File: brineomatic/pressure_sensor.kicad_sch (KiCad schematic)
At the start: 5 parts

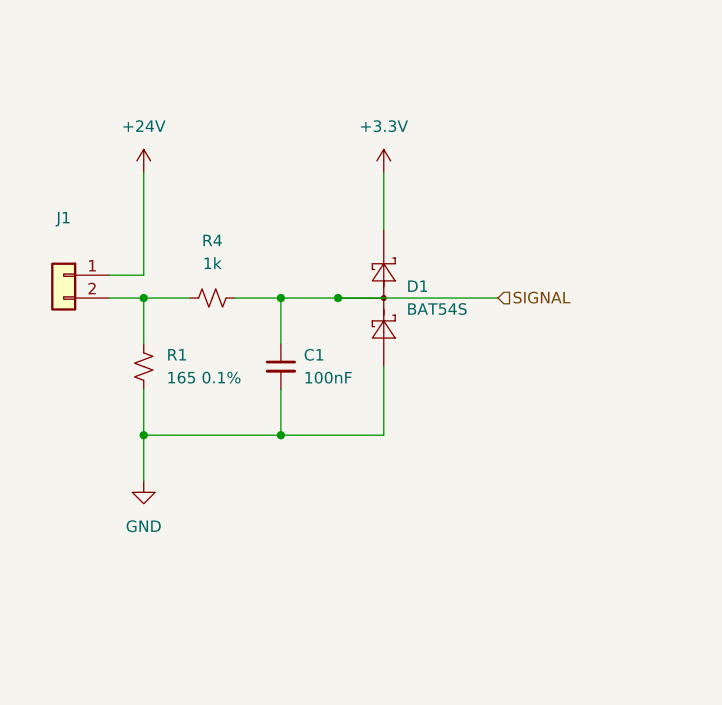
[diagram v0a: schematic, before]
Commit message: switched to onboard esp32-s3 and re-drew tmc2209 driver
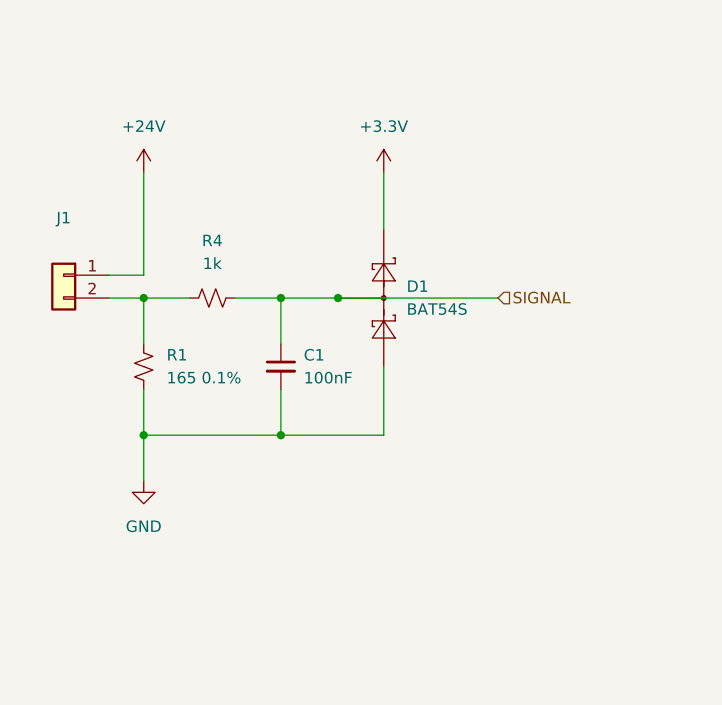
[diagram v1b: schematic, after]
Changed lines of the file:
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@@
 			)
 		)
-		(property "Description" ""
+		(property "Description" "Resistor, small US symbol"
 			(at 104.14 87.63 0)
 			(effects
@@
 		(fields_autoplaced yes)
 		(property "Reference" "R1"
-			(at 99.06 93.98 0)
+			(at 99.06 93.9799 0)
 			(effects
 				(font
@@
 		)
 		(property "Value" "165 0.1%"
-			(at 99.06 96.52 0)
+			(at 99.06 96.5199 0)
 			(effects
 				(font
@@
 			)
 		)
-		(property "Description" ""
+		(property "Description" "Resistor, small US symbol"
 			(at 96.52 95.25 0)
 			(effects

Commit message: tmc2209 driver schematic checked and laid out nicely.
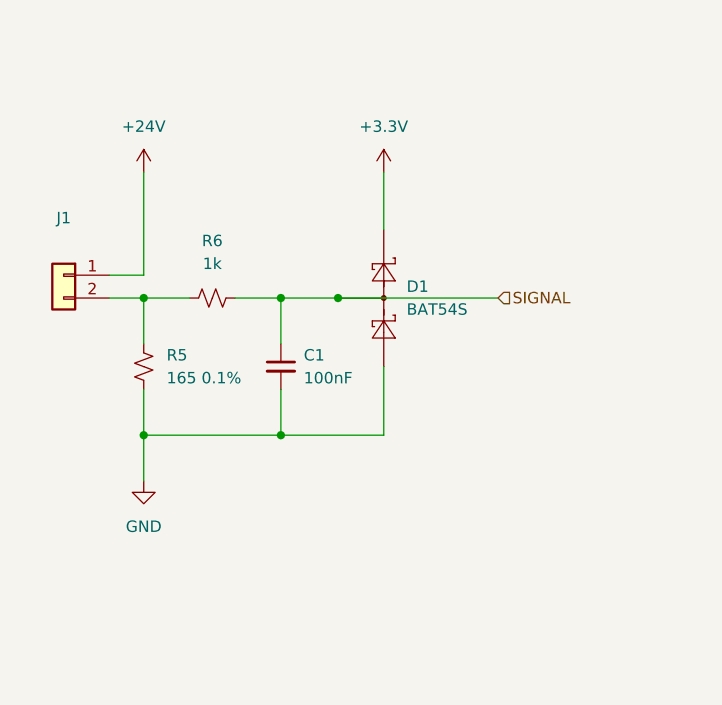
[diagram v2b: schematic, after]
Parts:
- renumbered R1 to R5, R4 to R6
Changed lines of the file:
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@@
 		(dnp no)
 		(fields_autoplaced yes)
-		(property "Reference" "#PWR06"
+		(property "Reference" "#PWR07"
 			(at 96.52 77.47 0)
 			(effects
@@
 			(project "brineomatic"
 				(path "/96477ae2-ef08-48f3-8dd4-fe4478541f68/c8ab4709-9ad5-4833-bb93-07e00d6a0170"
-					(reference "#PWR035")
-					(unit 1)
-				)
-				(path "/96477ae2-ef08-48f3-8dd4-fe4478541f68/e7fd98b0-0753-4e9e-b57d-135c0c1a0b39"
-					(reference "#PWR06")
+					(reference "#PWR039")
+					(unit 1)
+				)
+				(path "/96477ae2-ef08-48f3-8dd4-fe4478541f68/e7fd98b0-0753-4e9e-b57d-135c0c1a0b39"
+					(reference "#PWR07")
 					(unit 1)
 				)
@@
 		(dnp no)
 		(fields_autoplaced yes)
-		(property "Reference" "#PWR08"
+		(property "Reference" "#PWR09"
 			(at 123.19 77.47 0)
 			(effects
@@
 			(project "brineomatic"
 				(path "/96477ae2-ef08-48f3-8dd4-fe4478541f68/c8ab4709-9ad5-4833-bb93-07e00d6a0170"
-					(reference "#PWR037")
-					(unit 1)
-				)
-				(path "/96477ae2-ef08-48f3-8dd4-fe4478541f68/e7fd98b0-0753-4e9e-b57d-135c0c1a0b39"
-					(reference "#PWR08")
+					(reference "#PWR041")
+					(unit 1)
+				)
+				(path "/96477ae2-ef08-48f3-8dd4-fe4478541f68/e7fd98b0-0753-4e9e-b57d-135c0c1a0b39"
+					(reference "#PWR09")
 					(unit 1)
 				)
@@
 		(dnp no)
 		(fields_autoplaced yes)
-		(property "Reference" "#PWR07"
+		(property "Reference" "#PWR08"
 			(at 96.52 114.3 0)
 			(effects
@@
 			(project "brineomatic"
 				(path "/96477ae2-ef08-48f3-8dd4-fe4478541f68/c8ab4709-9ad5-4833-bb93-07e00d6a0170"
-					(reference "#PWR036")
-					(unit 1)
-				)
-				(path "/96477ae2-ef08-48f3-8dd4-fe4478541f68/e7fd98b0-0753-4e9e-b57d-135c0c1a0b39"
-					(reference "#PWR07")
+					(reference "#PWR040")
+					(unit 1)
+				)
+				(path "/96477ae2-ef08-48f3-8dd4-fe4478541f68/e7fd98b0-0753-4e9e-b57d-135c0c1a0b39"
+					(reference "#PWR08")
 					(unit 1)
 				)
@@
 			(project "brineomatic"
 				(path "/96477ae2-ef08-48f3-8dd4-fe4478541f68/c8ab4709-9ad5-4833-bb93-07e00d6a0170"
-					(reference "D18")
+					(reference "D19")
 					(unit 1)
 				)
@@
 			(project "brineomatic"
 				(path "/96477ae2-ef08-48f3-8dd4-fe4478541f68/c8ab4709-9ad5-4833-bb93-07e00d6a0170"
-					(reference "J12")
+					(reference "J17")
 					(unit 1)
 				)
@@
 		(dnp no)
 		(fields_autoplaced yes)
-		(property "Reference" "R4"
+		(property "Reference" "R6"
 			(at 104.14 81.28 90)
 			(effects
@@
 				)
 				(path "/96477ae2-ef08-48f3-8dd4-fe4478541f68/e7fd98b0-0753-4e9e-b57d-135c0c1a0b39"
-					(reference "R4")
+					(reference "R6")
 					(unit 1)
 				)
@@
 		(dnp no)
 		(fields_autoplaced yes)
-		(property "Reference" "R1"
+		(property "Reference" "R5"
 			(at 99.06 93.9799 0)
 			(effects
@@
 			(project "brineomatic"
 				(path "/96477ae2-ef08-48f3-8dd4-fe4478541f68/c8ab4709-9ad5-4833-bb93-07e00d6a0170"
-					(reference "R31")
-					(unit 1)
-				)
-				(path "/96477ae2-ef08-48f3-8dd4-fe4478541f68/e7fd98b0-0753-4e9e-b57d-135c0c1a0b39"
-					(reference "R1")
+					(reference "R33")
+					(unit 1)
+				)
+				(path "/96477ae2-ef08-48f3-8dd4-fe4478541f68/e7fd98b0-0753-4e9e-b57d-135c0c1a0b39"
+					(reference "R5")
 					(unit 1)
 				)
@@
 			(project "brineomatic"
 				(path "/96477ae2-ef08-48f3-8dd4-fe4478541f68/c8ab4709-9ad5-4833-bb93-07e00d6a0170"
-					(reference "C17")
-					(unit 1)
-				)
+					(reference "C14")
+					(unit 1)
+				)

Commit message: worked on bom for rev b prototype run
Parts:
- C1: LCSC C49678 -> (none)
- R6: LCSC C95781 -> (none)
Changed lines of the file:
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@@
 			)
 		)
-		(property "LCSC" "C95781"
+		(property "LCSC" ""
 			(at 104.14 87.63 0)
 			(effects
@@
 			)
 		)
-		(property "LCSC" "C49678"
+		(property "LCSC" ""
 			(at 111.76 95.25 0)
 			(effects

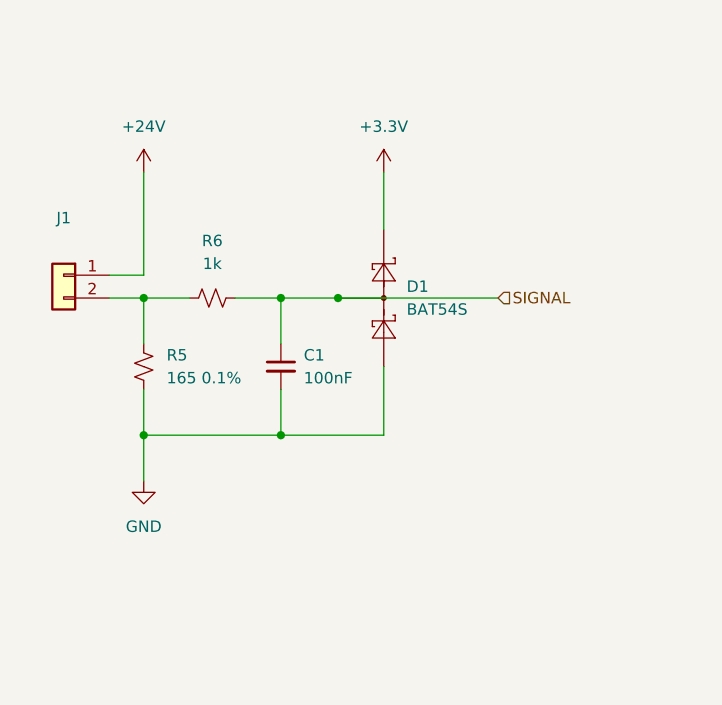
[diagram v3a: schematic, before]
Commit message: added qwiic i2c connector
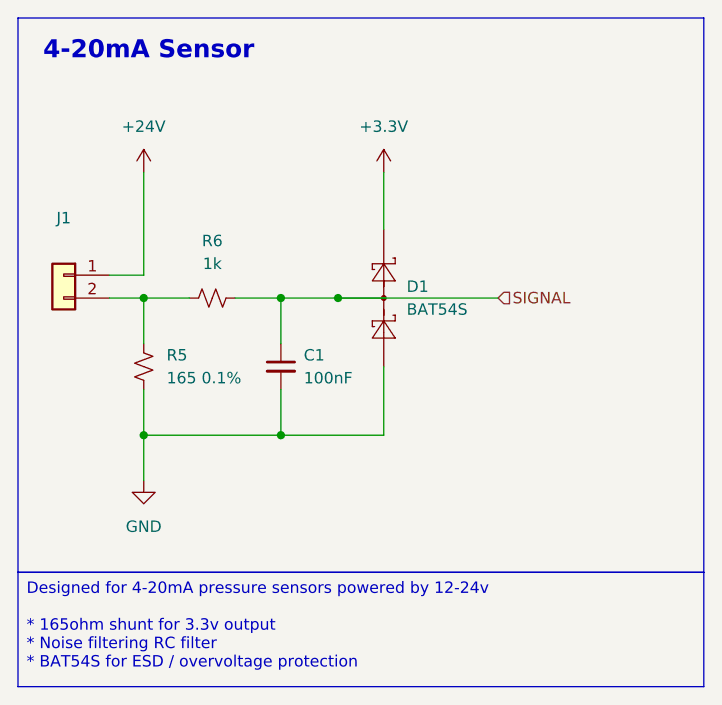
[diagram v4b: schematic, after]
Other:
- note added: "4-20mA Sensor"
- title: (none) -> https://github.com/hoeken/brineomatic
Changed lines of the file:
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@@
 	(generator_version "9.0")
 	(paper "A4")
+	(title_block
+		(title "https://github.com/hoeken/brineomatic")
+		(date "2025-08-28")
+		(rev "B")
+	)
+	(rectangle
+		(start 82.55 56.515)
+		(end 158.75 118.11)
+		(stroke
+			(width 0)
+			(type default)
+		)
+		(fill
+			(type none)
+		)
+	)
+	(text "4-20mA Sensor"
+		(exclude_from_sim no)
+		(at 85.344 60.198 0)
+		(effects
+			(font
+				(size 2 2)
+				(thickness 0.4)
+				(bold yes)
+			)
+			(justify left)
+		)
+	)
+	(text_box "Designed for 4-20mA pressure sensors powered by 12-24v\n\n* 165ohm shunt for 3.3v output\n* Noise filtering RC filter\n* BAT54S for ESD / overvoltage protection"
+		(exclude_from_sim no)
+		(at 82.55 118.11 0)
+		(size 76.2 12.7)
+		(margins 0.9525 0.9525 0.9525 0.9525)
+		(stroke
+			(width 0)
+			(type solid)
+		)
+		(fill
+			(type none)
+		)
+		(effects
+			(font
+				(size 1.27 1.27)
+			)
+			(justify left top)
+		)
+	)
 	(junction
 		(at 118.11 87.63)

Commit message: added pullup resistor to adc alert
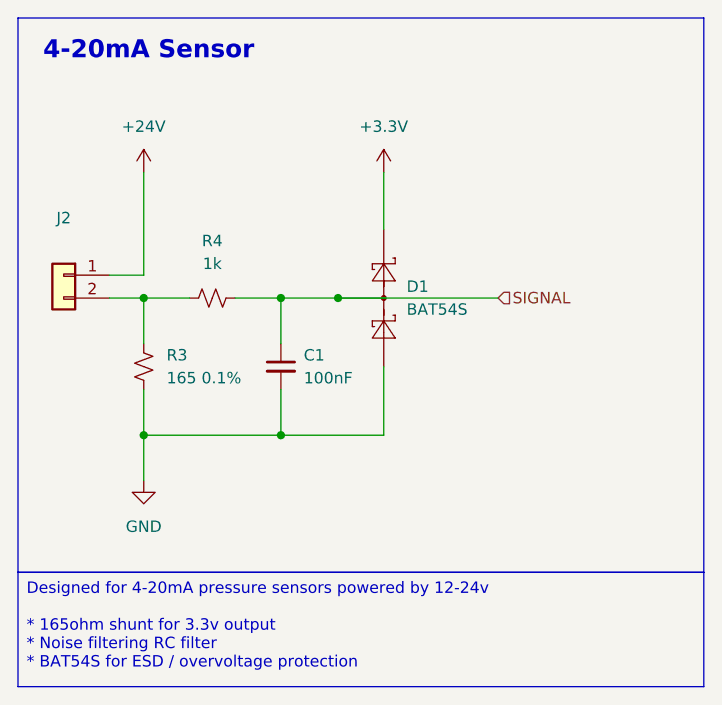
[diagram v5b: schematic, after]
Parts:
- renumbered J1 to J2, R5 to R3, R6 to R4
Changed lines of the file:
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@@
 		(dnp no)
 		(fields_autoplaced yes)
-		(property "Reference" "#PWR07"
+		(property "Reference" "#PWR09"
 			(at 96.52 77.47 0)
 			(effects
@@
 			(project "brineomatic"
 				(path "/96477ae2-ef08-48f3-8dd4-fe4478541f68/c8ab4709-9ad5-4833-bb93-07e00d6a0170"
-					(reference "#PWR039")
-					(unit 1)
-				)
-				(path "/96477ae2-ef08-48f3-8dd4-fe4478541f68/e7fd98b0-0753-4e9e-b57d-135c0c1a0b39"
-					(reference "#PWR07")
+					(reference "#PWR041")
+					(unit 1)
+				)
+				(path "/96477ae2-ef08-48f3-8dd4-fe4478541f68/e7fd98b0-0753-4e9e-b57d-135c0c1a0b39"
+					(reference "#PWR09")
 					(unit 1)
 				)
@@
 		(dnp no)
 		(fields_autoplaced yes)
-		(property "Reference" "#PWR09"
+		(property "Reference" "#PWR011"
 			(at 123.19 77.47 0)
 			(effects
@@
 			(project "brineomatic"
 				(path "/96477ae2-ef08-48f3-8dd4-fe4478541f68/c8ab4709-9ad5-4833-bb93-07e00d6a0170"
-					(reference "#PWR041")
-					(unit 1)
-				)
-				(path "/96477ae2-ef08-48f3-8dd4-fe4478541f68/e7fd98b0-0753-4e9e-b57d-135c0c1a0b39"
-					(reference "#PWR09")
+					(reference "#PWR043")
+					(unit 1)
+				)
+				(path "/96477ae2-ef08-48f3-8dd4-fe4478541f68/e7fd98b0-0753-4e9e-b57d-135c0c1a0b39"
+					(reference "#PWR011")
 					(unit 1)
 				)
@@
 		(dnp no)
 		(fields_autoplaced yes)
-		(property "Reference" "#PWR08"
+		(property "Reference" "#PWR010"
 			(at 96.52 114.3 0)
 			(effects
@@
 			(project "brineomatic"
 				(path "/96477ae2-ef08-48f3-8dd4-fe4478541f68/c8ab4709-9ad5-4833-bb93-07e00d6a0170"
-					(reference "#PWR040")
-					(unit 1)
-				)
-				(path "/96477ae2-ef08-48f3-8dd4-fe4478541f68/e7fd98b0-0753-4e9e-b57d-135c0c1a0b39"
-					(reference "#PWR08")
+					(reference "#PWR042")
+					(unit 1)
+				)
+				(path "/96477ae2-ef08-48f3-8dd4-fe4478541f68/e7fd98b0-0753-4e9e-b57d-135c0c1a0b39"
+					(reference "#PWR010")
 					(unit 1)
 				)
@@
 		(dnp no)
 		(fields_autoplaced yes)
-		(property "Reference" "J1"
+		(property "Reference" "J2"
 			(at 87.63 78.74 0)
 			(effects
@@
 			(project "brineomatic"
 				(path "/96477ae2-ef08-48f3-8dd4-fe4478541f68/c8ab4709-9ad5-4833-bb93-07e00d6a0170"
-					(reference "J17")
-					(unit 1)
-				)
-				(path "/96477ae2-ef08-48f3-8dd4-fe4478541f68/e7fd98b0-0753-4e9e-b57d-135c0c1a0b39"
-					(reference "J1")
+					(reference "J18")
+					(unit 1)
+				)
+				(path "/96477ae2-ef08-48f3-8dd4-fe4478541f68/e7fd98b0-0753-4e9e-b57d-135c0c1a0b39"
+					(reference "J2")
 					(unit 1)
 				)
@@
 		(dnp no)
 		(fields_autoplaced yes)
-		(property "Reference" "R6"
+		(property "Reference" "R4"
 			(at 104.14 81.28 90)
 			(effects
@@
 				)
 				(path "/96477ae2-ef08-48f3-8dd4-fe4478541f68/e7fd98b0-0753-4e9e-b57d-135c0c1a0b39"
-					(reference "R6")
+					(reference "R4")
 					(unit 1)
 				)
@@
 		(dnp no)
 		(fields_autoplaced yes)
-		(property "Reference" "R5"
+		(property "Reference" "R3"
 			(at 99.06 93.9799 0)
 			(effects
@@
 				)
 				(path "/96477ae2-ef08-48f3-8dd4-fe4478541f68/e7fd98b0-0753-4e9e-b57d-135c0c1a0b39"
-					(reference "R5")
+					(reference "R3")
 					(unit 1)
 				)
@@
 			(project "brineomatic"
 				(path "/96477ae2-ef08-48f3-8dd4-fe4478541f68/c8ab4709-9ad5-4833-bb93-07e00d6a0170"
-					(reference "C14")
-					(unit 1)
-				)
+					(reference "C15")
+					(unit 1)
+				)

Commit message: stacked tds, removed stepper vref, pulled in esp32-s3 schematic, added extra relay output
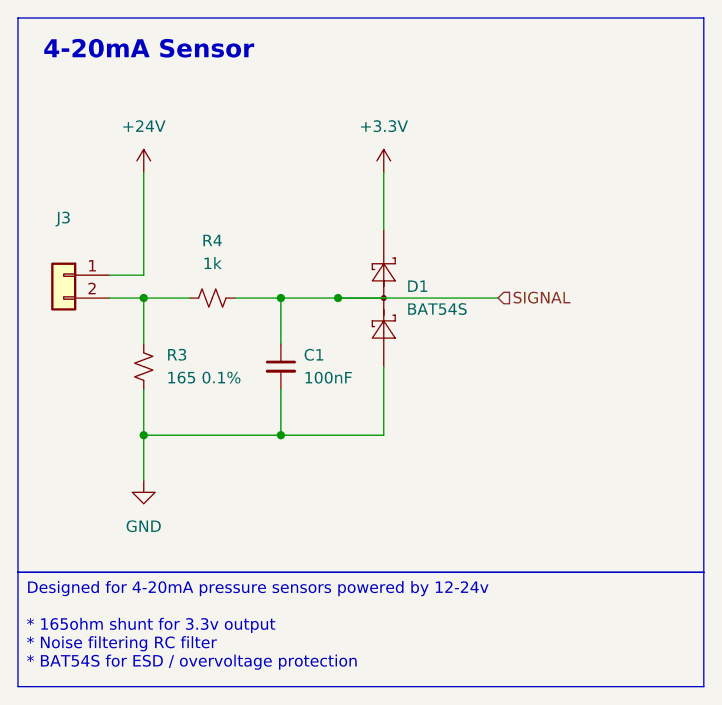
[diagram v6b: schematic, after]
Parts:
- renumbered J2 to J3
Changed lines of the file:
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@@
 		(dnp no)
 		(fields_autoplaced yes)
-		(property "Reference" "#PWR09"
+		(property "Reference" "#PWR011"
 			(at 96.52 77.47 0)
 			(effects
@@
 			(project "brineomatic"
 				(path "/96477ae2-ef08-48f3-8dd4-fe4478541f68/c8ab4709-9ad5-4833-bb93-07e00d6a0170"
-					(reference "#PWR041")
-					(unit 1)
-				)
-				(path "/96477ae2-ef08-48f3-8dd4-fe4478541f68/e7fd98b0-0753-4e9e-b57d-135c0c1a0b39"
-					(reference "#PWR09")
+					(reference "#PWR040")
+					(unit 1)
+				)
+				(path "/96477ae2-ef08-48f3-8dd4-fe4478541f68/e7fd98b0-0753-4e9e-b57d-135c0c1a0b39"
+					(reference "#PWR011")
 					(unit 1)
 				)
@@
 		(dnp no)
 		(fields_autoplaced yes)
-		(property "Reference" "#PWR011"
+		(property "Reference" "#PWR013"
 			(at 123.19 77.47 0)
 			(effects
@@
 			(project "brineomatic"
 				(path "/96477ae2-ef08-48f3-8dd4-fe4478541f68/c8ab4709-9ad5-4833-bb93-07e00d6a0170"
-					(reference "#PWR043")
-					(unit 1)
-				)
-				(path "/96477ae2-ef08-48f3-8dd4-fe4478541f68/e7fd98b0-0753-4e9e-b57d-135c0c1a0b39"
-					(reference "#PWR011")
+					(reference "#PWR042")
+					(unit 1)
+				)
+				(path "/96477ae2-ef08-48f3-8dd4-fe4478541f68/e7fd98b0-0753-4e9e-b57d-135c0c1a0b39"
+					(reference "#PWR013")
 					(unit 1)
 				)
@@
 		(dnp no)
 		(fields_autoplaced yes)
-		(property "Reference" "#PWR010"
+		(property "Reference" "#PWR012"
 			(at 96.52 114.3 0)
 			(effects
@@
 			(project "brineomatic"
 				(path "/96477ae2-ef08-48f3-8dd4-fe4478541f68/c8ab4709-9ad5-4833-bb93-07e00d6a0170"
-					(reference "#PWR042")
-					(unit 1)
-				)
-				(path "/96477ae2-ef08-48f3-8dd4-fe4478541f68/e7fd98b0-0753-4e9e-b57d-135c0c1a0b39"
-					(reference "#PWR010")
+					(reference "#PWR041")
+					(unit 1)
+				)
+				(path "/96477ae2-ef08-48f3-8dd4-fe4478541f68/e7fd98b0-0753-4e9e-b57d-135c0c1a0b39"
+					(reference "#PWR012")
 					(unit 1)
 				)
@@
 		(dnp no)
 		(fields_autoplaced yes)
-		(property "Reference" "J2"
+		(property "Reference" "J3"
 			(at 87.63 78.74 0)
 			(effects
@@
 				)
 				(path "/96477ae2-ef08-48f3-8dd4-fe4478541f68/e7fd98b0-0753-4e9e-b57d-135c0c1a0b39"
-					(reference "J2")
-					(unit 1)
-				)
+					(reference "J3")
+					(unit 1)
+				)
